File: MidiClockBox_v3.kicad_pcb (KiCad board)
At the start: 2 copper layers, 119.4 x 59.6 mm, 44 parts, among them J1 Midi In 0, J15 Conn_02x09_Odd_Even, J16 Conn_02x04_Odd_Even, J19 Conn_02x12_Counter_Clockwise, J2 ICSP, J20 Midi Out 0, J21 Midi Out 1, J22 Midi Out 2, J23 WS2812, J24 Display, J25 Midi Out 3, J26 Midi Out 4, J27 Midi Out 5, J28 Sync Out 0, J29 Sync Out 1, SW1 RotaryEncoder_Switch, U1 CD74HC4067SM, U2 74LS241, U3 6N138

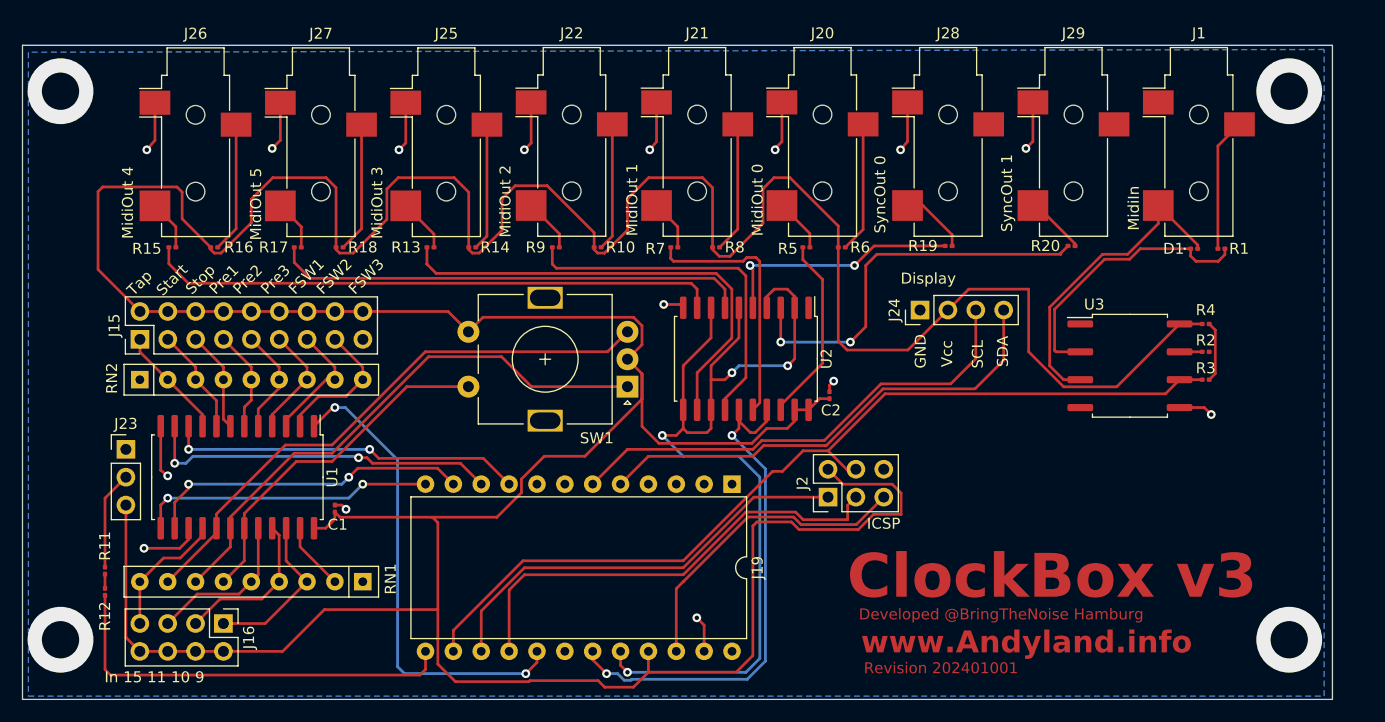
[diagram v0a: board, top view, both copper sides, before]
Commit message: switch resistor network for SMD parts
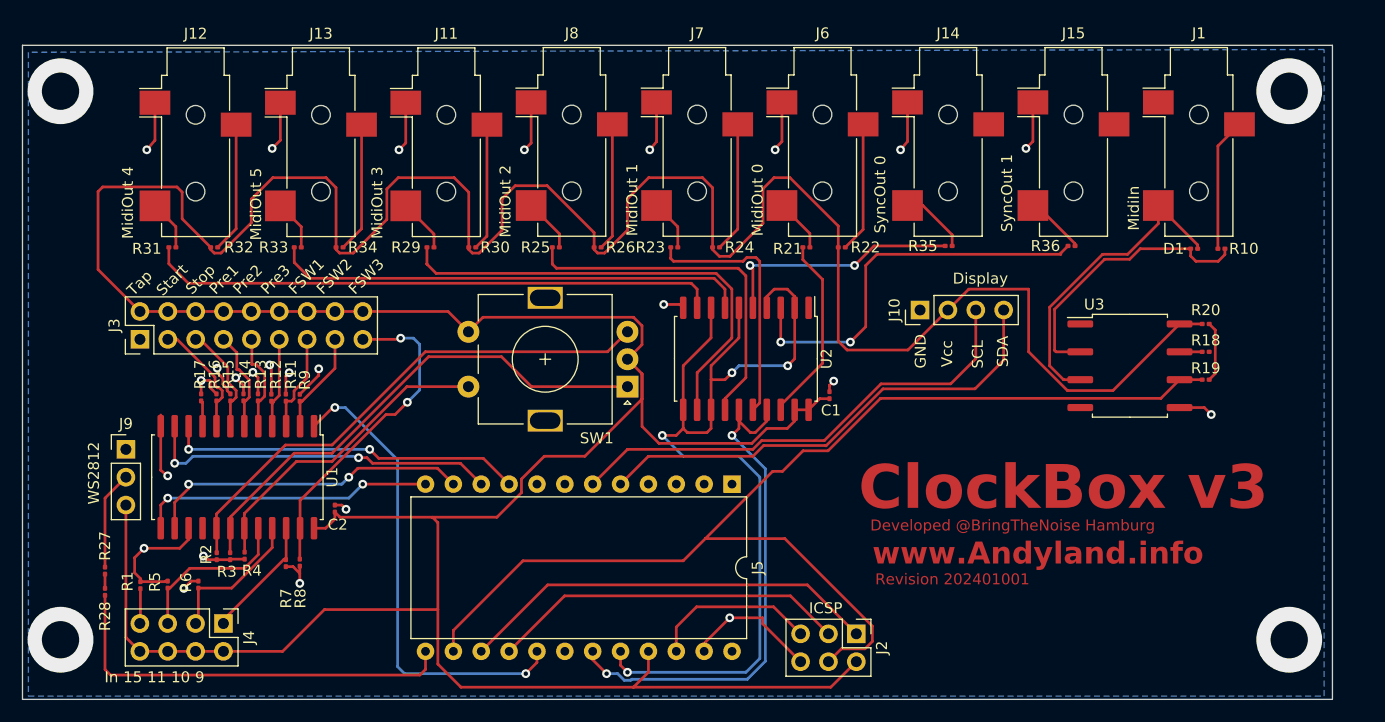
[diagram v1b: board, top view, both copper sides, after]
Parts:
- removed RN1, RN2: R_Network08, Resistor_THT:R_Array_SIP9
- added R1: 10k, Resistor_SMD:R_0201_0603Metric, F.Cu at (62.3, 93.0)
- added R11: 10k, Resistor_SMD:R_0201_0603Metric, F.Cu at (75.5, 75.9)
- added R12: 10k, Resistor_SMD:R_0201_0603Metric, F.Cu at (74.2, 75.9)
- added R13: 10k, Resistor_SMD:R_0201_0603Metric, F.Cu at (73.0, 75.9)
- added R14: 10k, Resistor_SMD:R_0201_0603Metric, F.Cu at (71.7, 75.9)
- added R15: 10k, Resistor_SMD:R_0201_0603Metric, F.Cu at (70.5, 75.9)
- added R16: 10k, Resistor_SMD:R_0201_0603Metric, F.Cu at (69.2, 75.9)
- added R17: 10k, Resistor_SMD:R_0201_0603Metric, F.Cu at (67.8, 75.9)
- added R2: 10k, Resistor_SMD:R_0201_0603Metric, F.Cu at (69.2, 90.4)
- added R3: 10k, Resistor_SMD:R_0201_0603Metric, F.Cu at (70.5, 90.4)
- added R4: 10k, Resistor_SMD:R_0201_0603Metric, F.Cu at (71.8, 90.3)
- added R5: 10k, Resistor_SMD:R_0201_0603Metric, F.Cu at (64.8, 93.0)
- added R6: 10k, Resistor_SMD:R_0201_0603Metric, F.Cu at (67.6, 93.0)
- added R7: 10k, Resistor_SMD:R_0201_0603Metric, F.Cu at (75.5, 91.0)
- added R8: 10k, Resistor_SMD:R_0201_0603Metric, F.Cu at (76.8, 91.0)
- added R9: 10k, Resistor_SMD:R_0201_0603Metric, F.Cu at (76.8, 75.9)
- moved J2 12.7 mm to (127.5, 97.5), turned to -90 degrees
- renumbered C2 to C1, C1 to C2, J24 to J10, J25 to J11, J26 to J12, J27 to J13, J28 to J14, J29 to J15, J15 to J3, J16 to J4, J19 to J5, J20 to J6, J21 to J7, J22 to J8, J23 to J9, R1 to R10, R2 to R18, R3 to R19, R4 to R20, R5 to R21, R6 to R22, R7 to R23, R8 to R24, R9 to R25, R10 to R26, R11 to R27, R12 to R28, R13 to R29, R14 to R30, R15 to R31, R16 to R32, R17 to R33, R18 to R34, R19 to R35, R20 to R36
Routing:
- net GND: track 58.0 -> 101.3 mm, vias 15 -> 25
- net +5V: track 426.7 -> 402.2 mm
- net IN_8: track 6.19 -> 30.1 mm, vias 0 -> 2
- net MIDI_RX: track 82.9 -> 104.3 mm
- net RST: track 28.6 -> 15.3 mm
- net SCLK: track 42.0 -> 32.6 mm
- net IN_0: track 10.3 -> 2.36 mm
- net IN_15: track 11.9 -> 4.31 mm
- net IN_14: track 52.4 -> 48.3 mm
- net IN_13: track 50.6 -> 46.6 mm
- net IN_12: track 32.2 -> 28.7 mm
- net IN_7: track 12.8 -> 9.38 mm
- net IN_9: track 14.9 -> 11.9 mm
- net IN_6: track 11.3 -> 9.04 mm
- net IN_5: track 10.3 -> 8.42 mm
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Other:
- board text added: "WS2812"

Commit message: switch SMD components form 0201-0603 to 0603-1608
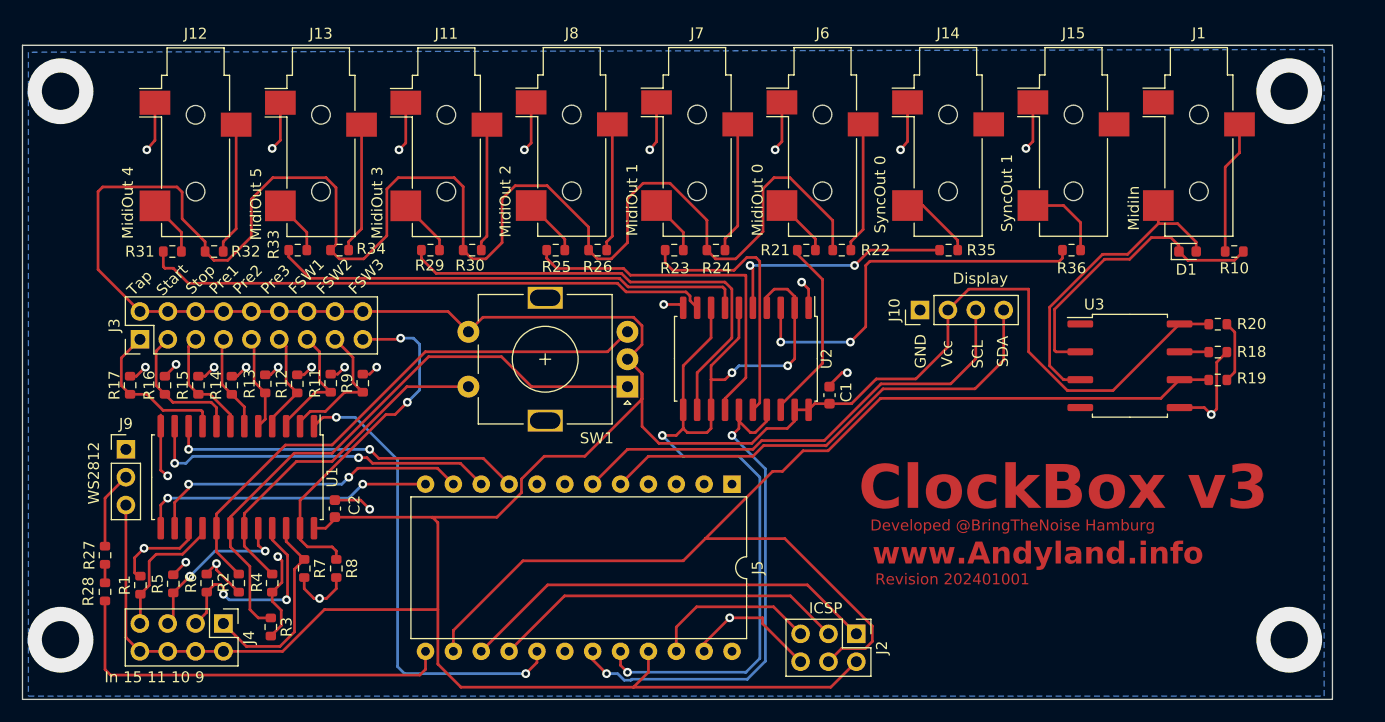
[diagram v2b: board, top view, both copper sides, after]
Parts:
- C1, C2: footprint Capacitor_SMD:C_0201_0603Metric -> Capacitor_SMD:C_0603_1608Metric
- D1: footprint Diode_SMD:D_0201_0603Metric -> Diode_SMD:D_0603_1608Metric
- R1, R10, R11, R12, R13, R14, R15, R16, R17, R18, R19, R2, R20, R21, R22, R23, R24, R25, R26, R27, R28, R29, R3, R30, R31, R32, R33, R34, R35, R36, R4, R5, R6, R7, R8, R9: footprint Resistor_SMD:R_0201_0603Metric -> Resistor_SMD:R_0603_1608Metric
- moved R3 7.44 mm to (74.2, 96.8)
- moved R17 6.57 mm to (61.3, 74.8)
- moved R9 5.89 mm to (82.5, 74.6)
- moved R16 4.83 mm to (64.5, 74.8)
- moved R11 4.30 mm to (79.6, 74.6)
- moved R4 3.55 mm to (74.3, 92.8)
- moved R8 3.37 mm to (80.1, 91.5)
- moved R2 3.17 mm to (71.2, 92.8)
- moved R15 3.12 mm to (67.6, 74.8)
- moved R12 2.68 mm to (76.6, 74.7)
- moved R7 1.75 mm to (77.2, 91.5)
- moved R14 1.53 mm to (70.6, 74.8)
- moved R27 1.40 mm to (59.1, 90.3)
- moved R13 1.40 mm to (73.7, 74.7)
- moved R10 1.20 mm to (162.0, 62.6)
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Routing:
- net GND: track 101.3 -> 116.9 mm, vias 25 -> 28
- net IN_0: track 2.36 -> 14.6 mm
- net IN_15: track 4.31 -> 13.1 mm
- net IN_13: track 46.6 -> 54.8 mm
- net IN_9: track 11.9 -> 18.7 mm
- net IN_10: track 13.4 -> 18.9 mm, vias 0 -> 2
- net IN_7: track 9.38 -> 13.1 mm
- net IN_12: track 28.7 -> 31.8 mm
- net IN_8: track 30.1 -> 32.8 mm
- net IN_14: track 48.3 -> 50.7 mm
- net IN_6: track 9.04 -> 11.3 mm
- net Net-(D1-K): track 25.6 -> 27.6 mm
- net Net-(J9-Pin_2): track 8.98 -> 7.08 mm
- net IN_1: track 10.9 -> 12.7 mm
- net Net-(J15-PadT): track 5.48 -> 7.12 mm
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
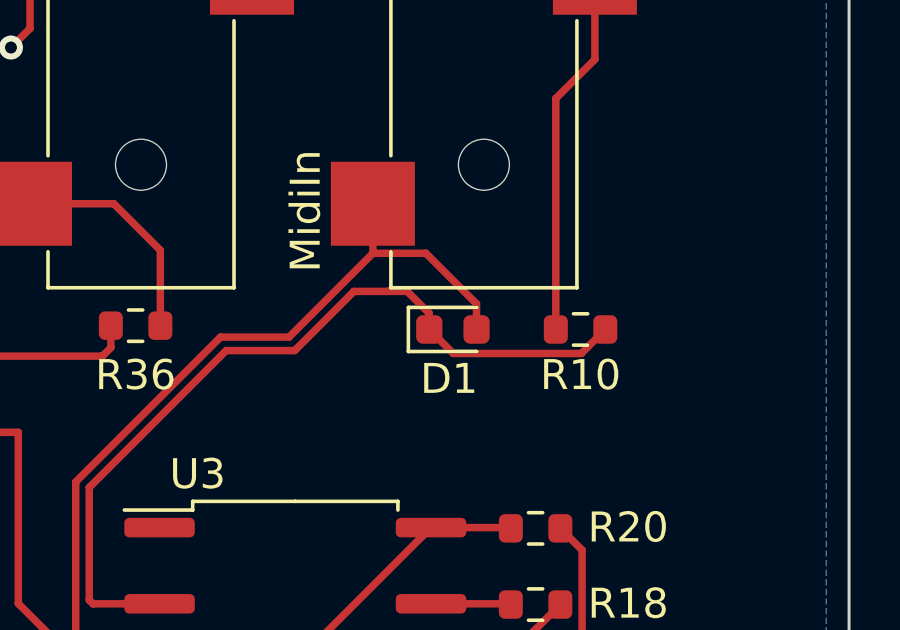
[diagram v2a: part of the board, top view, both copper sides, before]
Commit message: add centroid archive
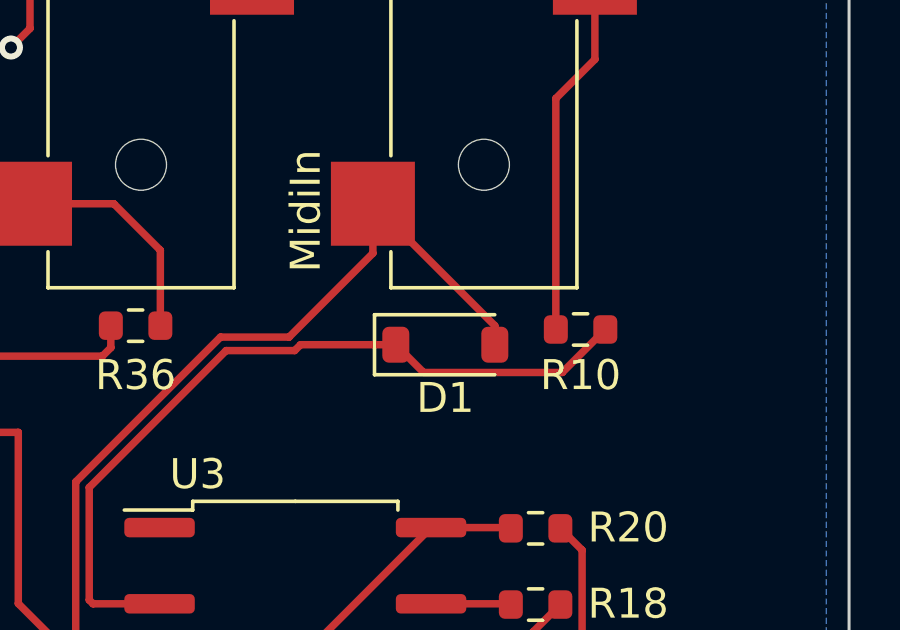
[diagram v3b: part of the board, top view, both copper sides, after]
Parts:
- D1: footprint Diode_SMD:D_0603_1608Metric -> Diode_SMD:D_SOD-123
- moved D1 0.57 mm to (157.5, 63.1)
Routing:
- net Net-(D1-A): track 28.4 -> 29.7 mm
- net Net-(D1-K): track 27.6 -> 26.3 mm
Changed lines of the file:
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@@
   (setup
     (pad_to_mask_clearance 0)
+    (aux_axis_origin 51.533056 103.435608)
     (pcbplotparams
       (layerselection 0x00010fc_ffffffff)
@@
       (outputformat 1)
       (mirror false)
-      (drillshape 1)
+      (drillshape 0)
       (scaleselection 1)
       (outputdirectory "")
@@
     )
   )
-  (footprint "Diode_SMD:D_0603_1608Metric" (layer "F.Cu")
-    (at 157.734 62.611)
-    (descr "Diode SMD 0603 (1608 Metric), square (rectangular) end terminal, IPC_7351 nominal, (Body size source: http://www.tortai-tech.com/upload/download/2011102023233369053.pdf), generated with kicad-footprint-generator")
-    (tags "diode")
+  (footprint "Diode_SMD:D_SOD-123" (layer "F.Cu")
+    (at 157.48 63.119)
+    (descr "SOD-123")
+    (tags "SOD-123")
     (property "Sheetfile" "MidiClockBox_v3.kicad_sch")
     (property "Sheetname" "")
@@
     (property "ki_keywords" "diode")
     (attr smd)
-    (fp_text reference "D1" (at -0.127 1.651) (layer "F.SilkS")
+    (fp_text reference "D1" (at 0 1.778) (layer "F.SilkS")
         (effects (font (size 1 1) (thickness 0.15)))
     )
-    (fp_text value "1N4148" (at 0 1.43) (layer "F.Fab")
+    (fp_text value "1N4148" (at 0 2.1) (layer "F.Fab")
         (effects (font (size 1 1) (thickness 0.15)))
     )
-    (fp_text user "${REFERENCE}" (at 0 0) (layer "F.Fab")
-        (effects (font (size 0.4 0.4) (thickness 0.06)))
+    (fp_text user "${REFERENCE}" (at 0 -2) (layer "F.Fab")
+        (effects (font (size 1 1) (thickness 0.15)))
     )
-    (fp_line (start -1.485 -0.735) (end -1.485 0.735)
+    (fp_line (start -2.36 -1) (end -2.36 1)
       (stroke (width 0.12) (type solid)) (layer "F.SilkS"))
-    (fp_line (start -1.485 0.735) (end 0.8 0.735)
+    (fp_line (start -2.36 -1) (end 1.65 -1)
       (stroke (width 0.12) (type solid)) (layer "F.SilkS"))
-    (fp_line (start 0.8 -0.735) (end -1.485 -0.735)
+    (fp_line (start -2.36 1) (end 1.65 1)
       (stroke (width 0.12) (type solid)) (layer "F.SilkS"))
-    (fp_line (start -1.48 -0.73) (end 1.48 -0.73)
+    (fp_line (start -2.35 -1.15) (end -2.35 1.15)
       (stroke (width 0.05) (type solid)) (layer "F.CrtYd"))
-    (fp_line (start -1.48 0.73) (end -1.48 -0.73)
+    (fp_line (start -2.35 -1.15) (end 2.35 -1.15)
       (stroke (width 0.05) (type solid)) (layer "F.CrtYd"))
-    (fp_line (start 1.48 -0.73) (end 1.48 0.73)
+    (fp_line (start 2.35 -1.15) (end 2.35 1.15)
       (stroke (width 0.05) (type solid)) (layer "F.CrtYd"))
-    (fp_line (start 1.48 0.73) (end -1.48 0.73)
+    (fp_line (start 2.35 1.15) (end -2.35 1.15)
       (stroke (width 0.05) (type solid)) (layer "F.CrtYd"))
-    (fp_line (start -0.8 -0.1) (end -0.8 0.4)
+    (fp_line (start -1.4 -0.9) (end 1.4 -0.9)
+      (stroke (width 0.1) (type solid)) (layer "F.Fab"))
+    (fp_line (start -1.4 0.9) (end -1.4 -0.9)
+      (stroke (width 0.1) (type solid)) (layer "F.Fab"))
+    (fp_line (start -0.75 0) (end -0.35 0)
+      (stroke (width 0.1) (type solid)) (layer "F.Fab"))
+    (fp_line (start -0.35 0) (end -0.35 -0.55)
+      (stroke (width 0.1) (type solid)) (layer "F.Fab"))
+    (fp_line (start -0.35 0) (end -0.35 0.55)
+      (stroke (width 0.1) (type solid)) (layer "F.Fab"))
+    (fp_line (start -0.35 0) (end 0.25 -0.4)
+      (stroke (width 0.1) (type solid)) (layer "F.Fab"))
+    (fp_line (start 0.25 -0.4) (end 0.25 0.4)
       (stroke (width 0.1) (type solid)) (layer "F.Fab"))
-    (fp_line (start -0.8 0.4) (end 0.8 0.4)
+    (fp_line (start 0.25 0) (end 0.75 0)
       (stroke (width 0.1) (type solid)) (layer "F.Fab"))
-    (fp_line (start -0.5 -0.4) (end -0.8 -0.1)
+    (fp_line (start 0.25 0.4) (end -0.35 0)
       (stroke (width 0.1) (type solid)) (layer "F.Fab"))
-    (fp_line (start 0.8 -0.4) (end -0.5 -0.4)
+    (fp_line (start 1.4 -0.9) (end 1.4 0.9)
       (stroke (width 0.1) (type solid)) (layer "F.Fab"))
-    (fp_line (start 0.8 0.4) (end 0.8 -0.4)
+    (fp_line (start 1.4 0.9) (end -1.4 0.9)
       (stroke (width 0.1) (type solid)) (layer "F.Fab"))
-    (pad "1" smd roundrect (at -0.7875 0) (size 0.875 0.95) (layers "F.Cu" "F.Paste" "F.Mask") (roundrect_rratio 0.25)
+    (pad "1" smd roundrect (at -1.65 0) (size 0.9 1.2) (layers "F.Cu" "F.Paste" "F.Mask") (roundrect_rratio 0.25)
       (net 3 "Net-(D1-K)") (pinfunction "K") (pintype "passive"))
-    (pad "2" smd roundrect (at 0.7875 0) (size 0.875 0.95) (layers "F.Cu" "F.Paste" "F.Mask") (roundrect_rratio 0.25)
+    (pad "2" smd roundrect (at 1.65 0) (size 0.9 1.2) (layers "F.Cu" "F.Paste" "F.Mask") (roundrect_rratio 0.25)
       (net 4 "Net-(D1-A)") (pinfunction "A") (pintype "passive"))
-    (model "${KICAD6_3DMODEL_DIR}/Diode_SMD.3dshapes/D_0603_1608Metric.wrl"
+    (model "${KICAD6_3DMODEL_DIR}/Diode_SMD.3dshapes/D_SOD-123.wrl"
       (offset (xyz 0 0 0))
       (scale (xyz 1 1 1))
@@
   (via (at 66.421 90.932) (size 0.8) (drill 0.4) (layers "F.Cu" "B.Cu") (net 2))
   (via (at 120.142 53.34) (size 0.8) (drill 0.4) (layers "F.Cu" "B.Cu") (net 2))
-  (segment (start 156.9465 62.0775) (end 156.9465 62.611) (width 0.25) (layer "F.Cu") (net 3))
-  (segment (start 152.459396 63.315) (end 154.432698 61.341698) (width 0.25) (layer "F.Cu") (net 3))
-  (segment (start 162.014 63.411) (end 157.7465 63.411) (width 0.25) (layer "F.Cu") (net 3))
   (segment (start 145.611 71.628) (end 145.611 67.877396) (width 0.25) (layer "F.Cu") (net 3))
   (segment (start 147.955 71.755) (end 145.738 71.755) (width 0.25) (layer "F.Cu") (net 3))
-  (segment (start 155.574302 61.341698) (end 155.575 61.341) (width 0.25) (layer "F.Cu") (net 3))
-  (segment (start 156.21 61.341) (end 156.9465 62.0775) (width 0.25) (layer "F.Cu") (net 3))
-  (segment (start 157.7465 63.411) (end 156.9465 62.611) (width 0.25) (layer "F.Cu") (net 3))
+  (segment (start 156.755 64.044) (end 161.381 64.044) (width 0.25) (layer "F.Cu") (net 3))
   (segment (start 145.738 71.755) (end 145.611 71.628) (width 0.25) (layer "F.Cu") (net 3))
-  (segment (start 154.432698 61.341698) (end 155.574302 61.341698) (width 0.25) (layer "F.Cu") (net 3))
-  (segment (start 155.575 61.341) (end 156.21 61.341) (width 0.25) (layer "F.Cu") (net 3))
-  (segment (start 162.814 62.611) (end 162.014 63.411) (width 0.25) (layer "F.Cu") (net 3))
+  (segment (start 152.655396 63.119) (end 155.83 63.119) (width 0.25) (layer "F.Cu") (net 3))
+  (segment (start 155.83 63.119) (end 156.755 64.044) (width 0.25) (layer "F.Cu") (net 3))
+  (segment (start 161.381 64.044) (end 162.814 62.611) (width 0.25) (layer "F.Cu") (net 3))
   (segment (start 150.173396 63.315) (end 152.459396 63.315) (width 0.25) (layer "F.Cu") (net 3))
   (segment (start 145.611 67.877396) (end 150.173396 63.315) (width 0.25) (layer "F.Cu") (net 3))
+  (segment (start 152.459396 63.315) (end 152.655396 63.119) (width 0.25) (layer "F.Cu") (net 3))
   (segment (start 155.067 60.071) (end 155.067 58.42) (width 0.25) (layer "F.Cu") (net 4))
   (segment (start 145.161 67.691) (end 149.987 62.865) (width 0.25) (layer "F.Cu") (net 4))
   (segment (start 149.987 62.865) (end 152.273 62.865) (width 0.25) (layer "F.Cu") (net 4))
   (segment (start 145.161 73.025) (end 145.161 67.691) (width 0.25) (layer "F.Cu") (net 4))
-  (segment (start 156.8345 60.071) (end 155.067 60.071) (width 0.25) (layer "F.Cu") (net 4))
   (segment (start 146.431 74.295) (end 145.161 73.025) (width 0.25) (layer "F.Cu") (net 4))
-  (segment (start 156.8345 60.071) (end 158.5215 61.758) (width 0.25) (layer "F.Cu") (net 4))
-  (segment (start 158.5215 61.758) (end 158.5215 62.611) (width 0.25) (layer "F.Cu") (net 4))
+  (segment (start 159.13 63.119) (end 159.13 62.483) (width 0.25) (layer "F.Cu") (net 4))
   (segment (start 152.273 62.865) (end 155.067 60.071) (width 0.25) (layer "F.Cu") (net 4))
+  (segment (start 159.13 62.483) (end 155.067 58.42) (width 0.25) (layer "F.Cu") (net 4))
   (segment (start 147.955 74.295) (end 146.431 74.295) (width 0.25) (layer "F.Cu") (net 4))
   (segment (start 161.164 62.611) (end 161.164 54.9106) (width 0.25) (layer "F.Cu") (net 5))
